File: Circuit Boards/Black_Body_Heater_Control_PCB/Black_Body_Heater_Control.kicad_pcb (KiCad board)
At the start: 2 copper layers, 57.5 x 42.8 mm, 43 parts, among them J1 USB_C_Receptacle_USB2.0_16P, J2 5040500891, J4 Conn_01x04_Pin, P1 436500200, P2 436500200, Q2 SI2310-TP, SW3 SW_MEC_5E, SW4 SW_MEC_5E, U1 ESP32-S3-WROOM-1-N8R8, U2 INA181A2IDBVR, U3 LMR51420XFDDCR, U4 USBLC6-2SC6, U5 AMS1117-3.3

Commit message: Updating silkscreen
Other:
- board text added: "12v - 24v VCC input"
- board text added: "BOOT"
- board text added: "Black Body Heater Controler REV. 0"
- board text added: "HEATER"
- board text added: "M2"
- board text added: "PROGRAMMER"
- board text added: "RESET"
- board text added: "TEMP SENSORS"
- board text added: "UART"
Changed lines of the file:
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@@
 		(capping no)
 		(filling no)
+		(zone_defaults)
 		(pcbplotparams
 			(layerselection 0x00000000_00000000_55555555_5755f5ff)
@@
 		(sheetname "/ESP32/")
 		(sheetfile "ESP32.kicad_sch")
-		(units
-			(unit
-				(name "A")
-				(pins "1" "2" "3" "4" "5" "6" "7" "8")
-			)
-		)
 		(attr smd)
 		(duplicate_pad_numbers_are_jumpers no)
@@
 			(layer "F.SilkS")
 		)
-		(fp_circle
-			(center 9.518701 3.042001)
-			(end 9.899701 3.042001)
-			(stroke
-				(width 0.508)
-				(type solid)
-			)
-			(fill no)
-			(layer "F.SilkS")
-		)
-		(fp_circle
-			(center 9.518701 3.042001)
-			(end 9.899701 3.042001)
-			(stroke
-				(width 0.508)
-				(type solid)
-			)
-			(fill no)
-			(layer "B.SilkS")
-		)
 		(fp_line
 			(start -8.756701 3.816701)
@@
 		(layer "Edge.Cuts")
 	)
+	(gr_text "UART"
+		(at 86.5 88.5 0)
+		(layer "F.SilkS")
+		(effects
+			(font
+				(size 1 1)
+				(thickness 0.2)
+				(bold yes)
+			)
+			(justify bottom)
+		)
+	)
+	(gr_text "HEATER"
+		(at 87.5 105 0)
+		(layer "F.SilkS")
+		(effects
+			(font
+				(size 1 1)
+				(thickness 0.2)
+				(bold yes)
+			)
+			(justify bottom)
+		)
+	)
+	(gr_text "PROGRAMMER"
+		(at 88 102.5 0)
+		(layer "F.SilkS")
+		(effects
+			(font
+				(size 1 1)
+				(thickness 0.2)
+				(bold yes)
+			)
+			(justify bottom)
+		)
+	)
+	(gr_text "RESET"
+		(at 93 92 0)
+		(layer "F.SilkS")
+		(effects
+			(font
+				(size 1 1)
+				(thickness 0.2)
+				(bold yes)
+			)
+			(justify bottom)
+		)
+	)
+	(gr_text "BOOT"
+		(at 126.5 92 0)
+		(layer "F.SilkS")
+		(effects
+			(font
+				(size 1 1)
+				(thickness 0.2)
+				(bold yes)
+			)
+			(justify bottom)
+		)
+	)
+	(gr_text "12v - 24v\nVCC input"
+		(at 130 112 90)
+		(layer "F.SilkS")
+		(effects
+			(font
+				(size 1 1)
+				(thickness 0.2)
+				(bold yes)
+			)
+			(justify bottom)
+		)
+	)
+	(gr_text "TEMP SENSORS"
+		(at 131.5 95 90)
+		(layer "F.SilkS")
+		(effects
+			(font
+				(size 1 1)
+				(thickness 0.2)
+				(bold yes)
+			)
+			(justify bottom)
+		)
+	)
+	(gr_text "M2"
+		(at 88 116 0)
+		(layer "B.SilkS")
+		(effects
+			(font
+				(size 1 1)
+				(thickness 0.15)
+			)
+			(justify left bottom mirror)
+		)
+	)
+	(gr_text "M2"
+		(at 92 84.5 0)
+		(layer "B.SilkS")
+		(effects
+			(font
+				(size 1 1)
+				(thickness 0.15)
+			)
+			(justify left bottom mirror)
+		)
+	)
+	(gr_text "M2"
+		(at 133 84.5 0)
+		(layer "B.SilkS")
+		(effects
+			(font
+				(size 1 1)
+				(thickness 0.15)
+			)
+			(justify left bottom mirror)
+		)
+	)
+	(gr_text "M2"
+		(at 137 116 0)
+		(layer "B.SilkS")
+		(effects
+			(font
+				(size 1 1)
+				(thickness 0.15)
+			)
+			(justify left bottom mirror)
+		)
+	)
+	(gr_text "Black Body Heater Controler REV. 0"
+		(at 132.5 120 0)
+		(layer "B.SilkS")
+		(effects
+			(font
+				(size 1.5 1.5)
+				(bold yes)
+			)
+			(justify left bottom mirror)
+		)
+	)
+	(gr_text_box "Programming Mode:\n1. Hold BOOT\n2. Press RESET\n3. Release RESET\n3. Release BOOT"
+		(start 127.429362 88.5)
+		(end 137.570638 105.5)
+		(margins 1.0025 1.0025 1.0025 1.0025)
+		(angle 90)
+		(layer "B.SilkS")
+		(effects
+			(font
+				(size 1 1)
+				(thickness 0.15)
+			)
+			(justify left top mirror)
+		)
+		(border yes)
+		(stroke
+			(width 0.15)
+			(type solid)
+		)
+		(knockout no)
+	)
 	(via

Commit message: Complete except for recommended changes
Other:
- board text removed: "M2"
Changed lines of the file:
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@@
 		(capping no)
 		(filling no)
-		(zone_defaults)
 		(pcbplotparams
 			(layerselection 0x00000000_00000000_55555555_5755f5ff)
@@
 		)
 	)
-	(gr_text "M2"
-		(at 88 116 0)
-		(layer "B.SilkS")
-		(effects
-			(font
-				(size 1 1)
-				(thickness 0.15)
-			)
-			(justify left bottom mirror)
-		)
-	)
-	(gr_text "M2"
-		(at 92 84.5 0)
-		(layer "B.SilkS")
-		(effects
-			(font
-				(size 1 1)
-				(thickness 0.15)
-			)
-			(justify left bottom mirror)
-		)
-	)
-	(gr_text "M2"
-		(at 133 84.5 0)
-		(layer "B.SilkS")
-		(effects
-			(font
-				(size 1 1)
-				(thickness 0.15)
-			)
-			(justify left bottom mirror)
-		)
-	)
-	(gr_text "M2"
-		(at 137 116 0)
-		(layer "B.SilkS")
-		(effects
-			(font
-				(size 1 1)
-				(thickness 0.15)
-			)
-			(justify left bottom mirror)
-		)
-	)

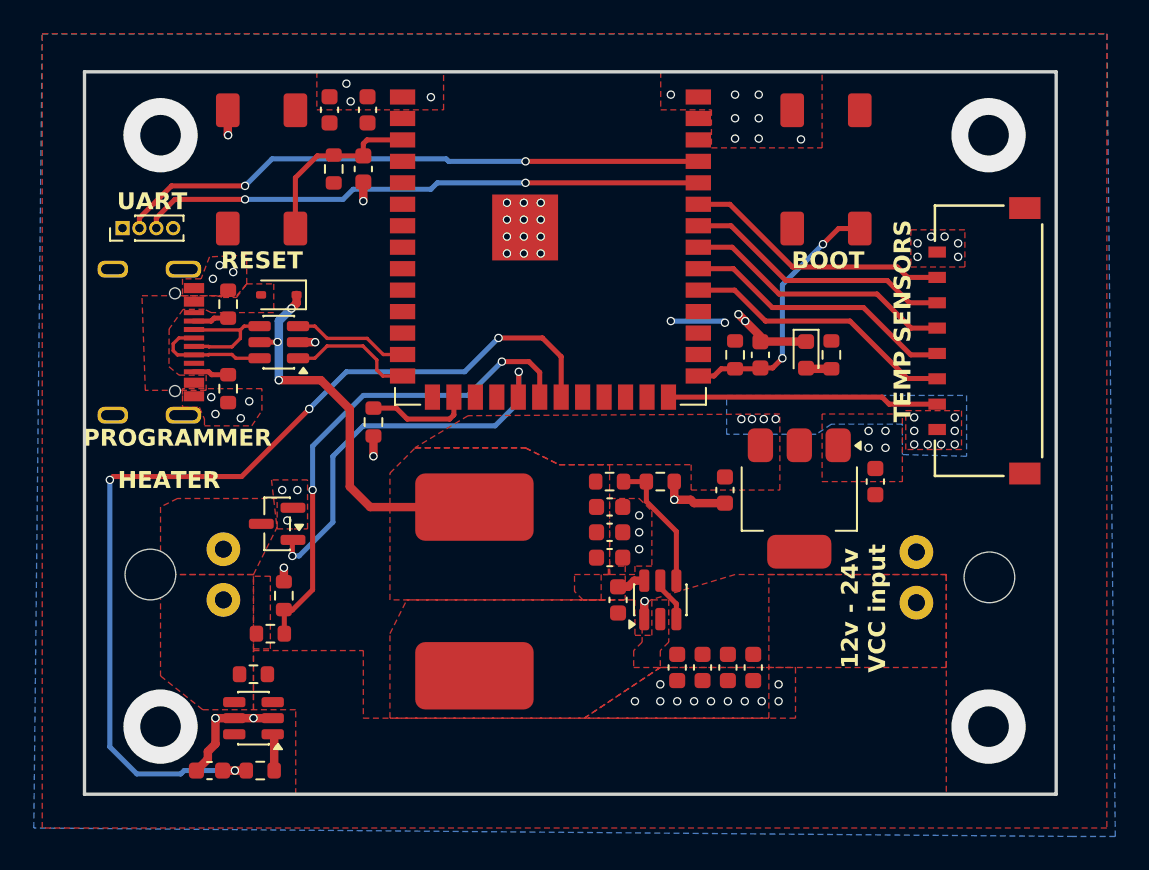
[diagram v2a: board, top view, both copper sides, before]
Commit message: Heater switched from pwm to vccs
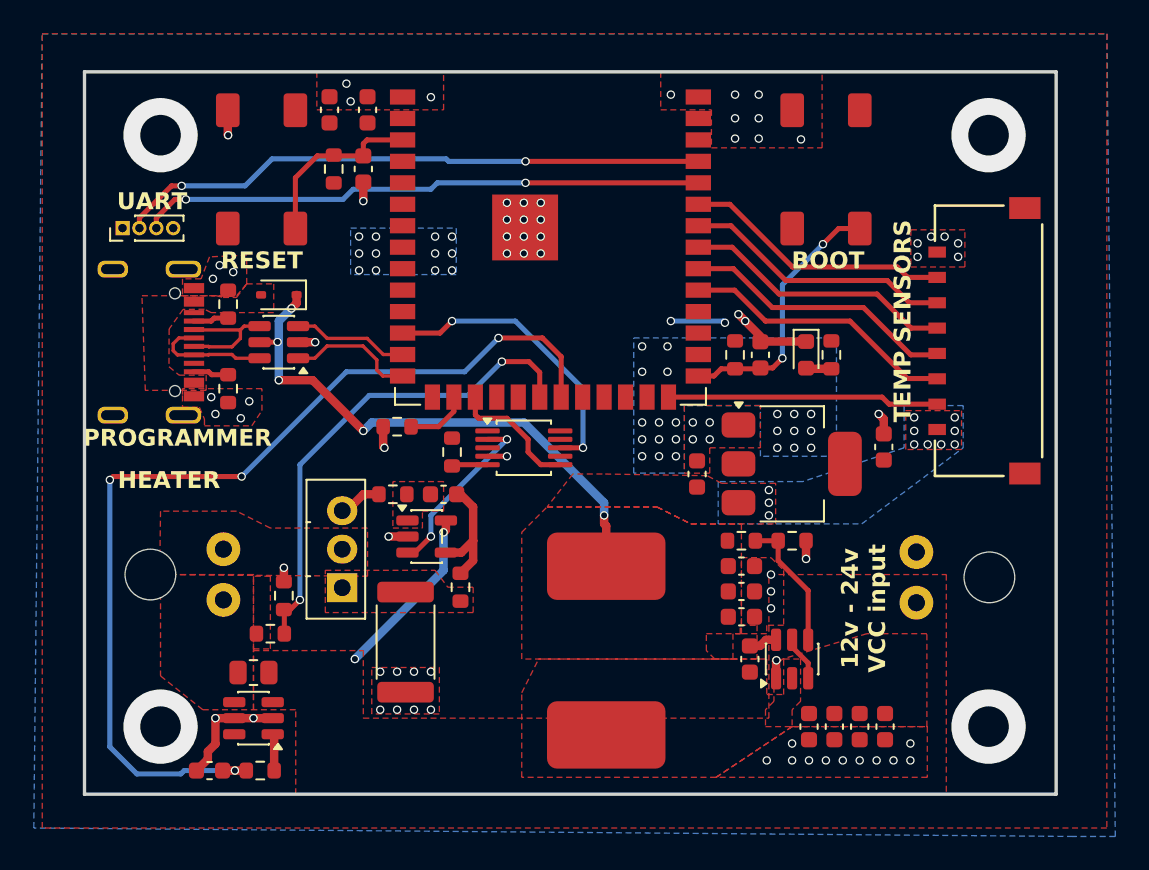
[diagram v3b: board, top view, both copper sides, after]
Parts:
- removed Q2: SI2310-TP, Package_TO_SOT_SMD:SOT-23
- added C301: 100nf, Capacitor_SMD:C_0603_1608Metric, F.Cu at (103.8, 105.2)
- added Q302: BD139, Package_TO_SOT_THT:TO-126-3_Vertical, F.Cu at (97.8, 110.8)
- added R302: 1k, Resistor_SMD:R_0603_1608Metric, F.Cu at (104.2, 102.8)
- added R304: 1k, Resistor_SMD:R_0603_1608Metric, F.Cu at (104.8, 110.8)
- added R305: 1k, Resistor_SMD:R_0603_1608Metric, F.Cu at (100.8, 105.2)
- added R306: 10, Resistor_SMD:R_2512_6332Metric, F.Cu at (101.5, 114.0)
- added U301: DAC60501ZDGSR, Package_SO:TSSOP-10_3x3mm_P0.5mm, F.Cu at (108.5, 102.5)
- added U303: TLV9061xDBV, Package_TO_SOT_SMD:SOT-23-5, F.Cu at (102.8, 107.8)
- D201: renamed from D2; value LED -> RED
- R301: renamed from R1; footprint Resistor_SMD:R_0603_1608Metric -> Resistor_SMD:R_0805_2012Metric
- moved C302 8.55 mm to (129.9, 119.0)
- moved C303 8.55 mm to (126.9, 119.0)
- moved C304 8.55 mm to (128.4, 119.0)
- moved C305 8.55 mm to (125.4, 119.0)
- moved C306 8.55 mm to (121.9, 115.0)
- moved C307 8.55 mm to (121.4, 111.0)
- moved C308 8.55 mm to (121.4, 112.5)
- moved C309 8.55 mm to (121.4, 109.5)
- moved L301 8.55 mm to (113.4, 114.5)
- moved R309 8.55 mm to (121.4, 108.0)
- moved R310 8.55 mm to (124.4, 108.0)
- moved U304 8.55 mm to (124.4, 115.0)
- moved C203 2.11 mm to (129.8, 102.5)
- moved U201 2.10 mm to (124.3, 103.5), turned to 0 degrees
- moved C201 1.90 mm to (118.8, 104.0), turned to 90 degrees
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- renumbered C14 to C201, C10 to C202, C8 to C203, C9 to C204, C15 to C205, C7 to C206, C6 to C207, C4 to C302, C3 to C303, C2 to C304, C1 to C305, C5 to C306, C11 to C307, C12 to C308, C13 to C309, D1 to D202, J2 to J201, J4 to J202, J1 to J203, L1 to L301, P1 to P301, P2 to P302, R10 to R201, R6 to R202, R9 to R203, R12 to R204, R11 to R205, R7 to R206, R8 to R207, R2 to R307, R3 to R308, R4 to R309, R5 to R310, SW4 to SW201, SW3 to SW202, U5 to U201, U1 to U202, U4 to U203, U2 to U302, U3 to U304
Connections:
- U202 pad 12: unconnected-(U1-IO8-Pad12) -> /ESP32/i2c.sda
- U202 pad 17: unconnected-(U1-IO9-Pad17) -> /ESP32/i2c.scl
- U202 pad 19: /ESP32/FET -> unconnected-(U202-IO11-Pad19)
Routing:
- net /ESP32/FET: track 23.5 -> 0.00 mm, vias 2 -> 0
- net /ESP32/i2c.sda: track 0.00 -> 17.5 mm, vias 0 -> 2
- net /Power_periferals/vout: track 0.00 -> 10.5 mm, vias 0 -> 2
- net VCC: track 2.24 -> 12.7 mm, vias 0 -> 2
- net +5V: track 23.9 -> 33.0 mm, vias 15 -> 16
- net /ESP32/i2c.scl: track 0.00 -> 7.73 mm
- net /Power_periferals/neg_fdbk: track 0.00 -> 7.42 mm
- net /Power_periferals/fet_in: track 0.00 -> 2.58 mm
- net /ESP32/IO46: track 6.18 -> 3.75 mm
- net /Power_periferals/i2c: track 0.00 -> 1.67 mm
- net GND: track 22.7 -> 23.3 mm, vias 68 -> 76
- net +3V3: vias 2 -> 36
- added copper zone on B.Cu, net +3V3
- added copper zone on F.Cu, net /Power_periferals/npn_gnd
- added copper zone on F.Cu, net /Power_periferals/opamp_out

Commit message: heater ready to order
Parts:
- added C310: 100nf, Capacitor_SMD:C_0603_1608Metric, F.Cu at (95.6, 119.4)
- added C311: 100nf, Capacitor_SMD:C_0603_1608Metric, F.Cu at (102.0, 102.8)
- added C312: 100nf, Capacitor_SMD:C_0603_1608Metric, F.Cu at (113.2, 101.4)
- added R303: 5.1k, Resistor_SMD:R_0603_1608Metric, F.Cu at (108.6, 105.0)
- added R311: 5.1k, Resistor_SMD:R_0603_1608Metric, F.Cu at (113.2, 102.9)
- R306: value 10 -> 5.1
- moved R205 1.00 mm to (102.0, 101.3)
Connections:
- U301 pad 10: +3V3 -> /Power_periferals/vrefIO
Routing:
- net +3V3: track 3.24 -> 9.53 mm, vias 36 -> 38
- net GND: track 23.3 -> 28.0 mm, vias 76 -> 77
- net /ESP32/i2c.scl: track 7.73 -> 10.5 mm
- net /ESP32/i2c.sda: track 17.5 -> 19.5 mm
- net /Power_periferals/vrefIO: track 0.00 -> 1.82 mm
- net /ESP32/IO46: track 3.75 -> 2.78 mm
- net VCC: vias 2 -> 14
- added copper zone on B.Cu, net VCC
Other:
- board text added: "- +"
- board text added: "3V3 Tx Rx GND"
- board text added: "GND VCC"

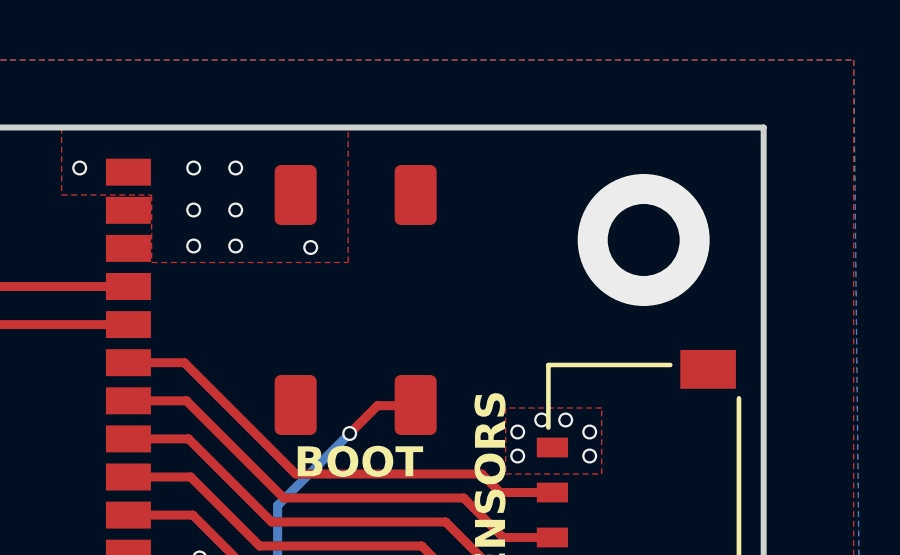
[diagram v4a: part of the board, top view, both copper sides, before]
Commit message: Temp probe bom done
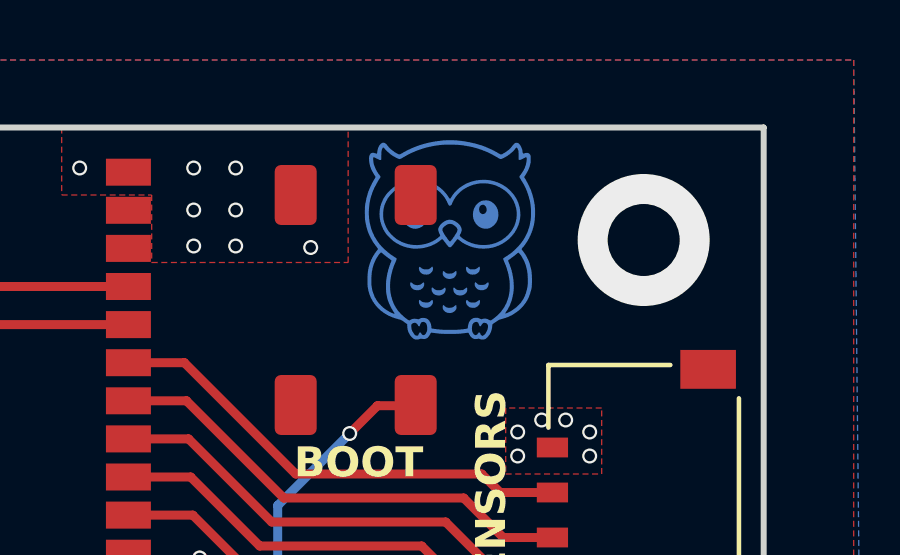
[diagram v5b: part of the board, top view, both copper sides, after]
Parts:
- added ?: LOGO, LOGO, B.Cu at (129.5, 84.0)

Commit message: Designs finished - order placed
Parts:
- removed U303: TLV9061xDBV, Package_TO_SOT_SMD:SOT-23-5
- added D301: SMAJ24A, Diode_SMD:D_SMA, F.Cu at (128.4, 110.6)
- added U305: LM358, Package_SO:SOIC-8_3.9x4.9mm_P1.27mm, F.Cu at (102.0, 109.7)
- R202, R302: value 1k -> 1.33k
- R206, R207, R303, R311: footprint Resistor_SMD:R_0603_1608Metric -> Resistor_SMD:R_0402_1005Metric
- R304, R305: value 1k -> 500
- R310: value 22.1k -> 22.6k
- moved R306 3.39 mm to (101.9, 117.4)
- moved R304 3.08 mm to (105.2, 113.8)
- moved R206 0.84 mm to (90.8, 94.8), turned to 0 degrees
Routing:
- net VCC: track 12.7 -> 2.24 mm, vias 14 -> 12
- net /Power_periferals/neg_fdbk: track 7.42 -> 13.0 mm
- net /Power_periferals/opamp_out: track 0.00 -> 3.76 mm
- net GND: track 28.0 -> 29.4 mm, vias 77 -> 78
- net /Power_periferals/vout: track 10.5 -> 11.9 mm
- net /ESP32/CC1: track 2.13 -> 1.34 mm
- removed copper zone on F.Cu, net /Power_periferals/opamp_out
